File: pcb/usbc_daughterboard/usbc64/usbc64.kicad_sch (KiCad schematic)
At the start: 14 parts, among them J1 C-31-M12, J2 JST SH, U1 ESDALD05UG4

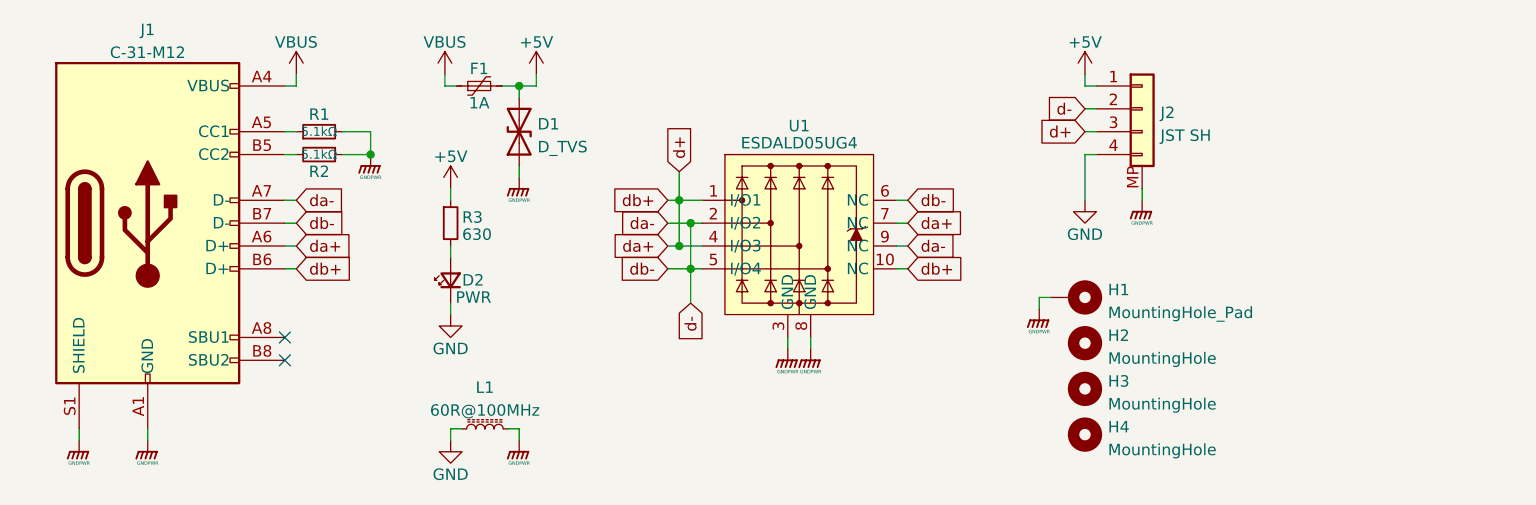
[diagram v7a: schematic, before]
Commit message: Ω symbol for resistor value
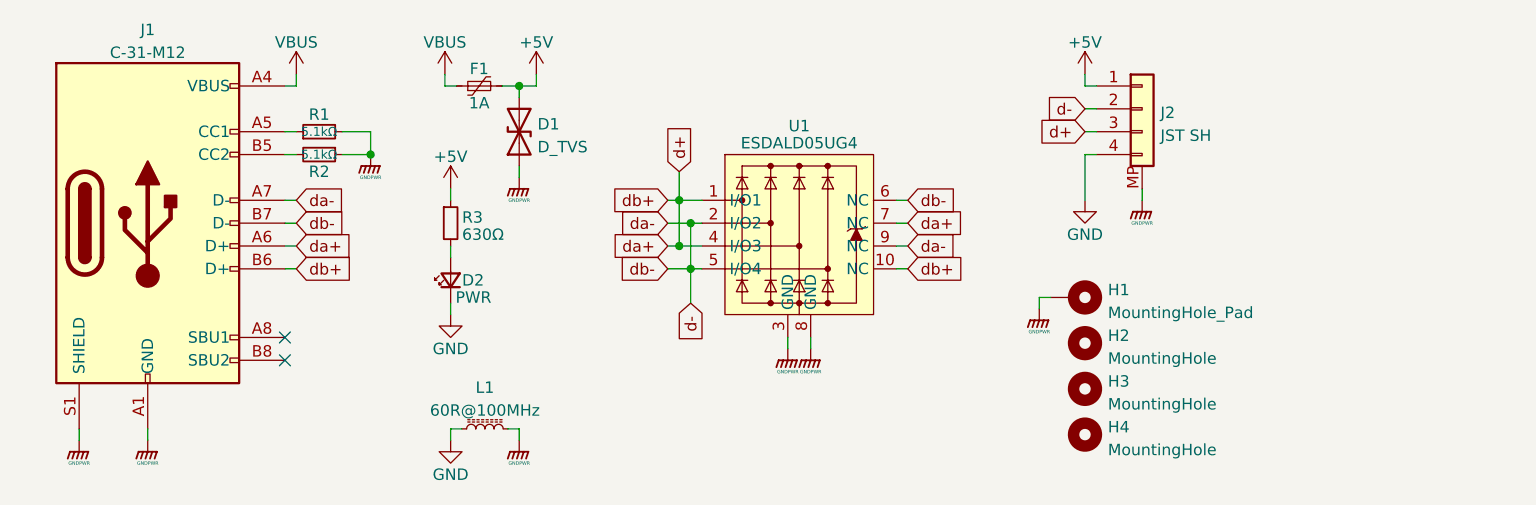
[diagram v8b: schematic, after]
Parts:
- R3: value 630 -> 630Ω
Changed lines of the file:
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@@
       (effects (font (size 1.27 1.27)) (justify left))
     )
-    (property "Value" "630" (id 1) (at 83.82 59.055 0)
+    (property "Value" "630Ω" (id 1) (at 83.82 59.055 0)
       (effects (font (size 1.27 1.27)) (justify left))
     )
@@
     )
     (path "/4af9b030-0adb-4a95-8fdf-1aa55ca1db80"
-      (reference "R3") (unit 1) (value "630") (footprint "Resistor_SMD:R_0603_1608Metric")
+      (reference "R3") (unit 1) (value "630Ω") (footprint "Resistor_SMD:R_0603_1608Metric")
     )
     (path "/a6f9bf39-ab6c-4e85-8e29-1b6c85263359"
